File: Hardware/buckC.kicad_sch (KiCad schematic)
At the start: 33 parts, among them Q1 SSM3K15AMFV,L3F, U6 SiC437BED-T1-GE3

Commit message: Maybe chad v3.0 hardware
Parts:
- added C18: TBD, Capacitor_SMD:C_0603_1608Metric, symbol Device:C_Small
- added C19: 47uF, Capacitor_SMD:C_1206_3216Metric, symbol Device:C_Small
- added R42: TBD, Resistor_SMD:R_0603_1608Metric, symbol Device:R_Small
- C31, C34, C36, C40, C41, C42, C43, C44, C47, C49: value DNP -> 47uF; now not fitted
- C46, C48: value DNP -> 47uF; footprint Capacitor_SMD:C_0805_2012Metric -> Capacitor_SMD:C_1206_3216Metric; now not fitted
- L4: MPN (none) -> SPM10065VT-3R3M-D
- U6: value SiC437BED-T1-GE3 -> SiC437AED-T1
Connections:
- net +6V: now also C19.2
- net GND: now also C19.1, R42.2
- net SW: now also C18.1
- net +12V renamed +16.8V
- new net: C18.2, R42.1
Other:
- note added: "RC Snubber"
- moved on the sheet: Q1, R38, R39

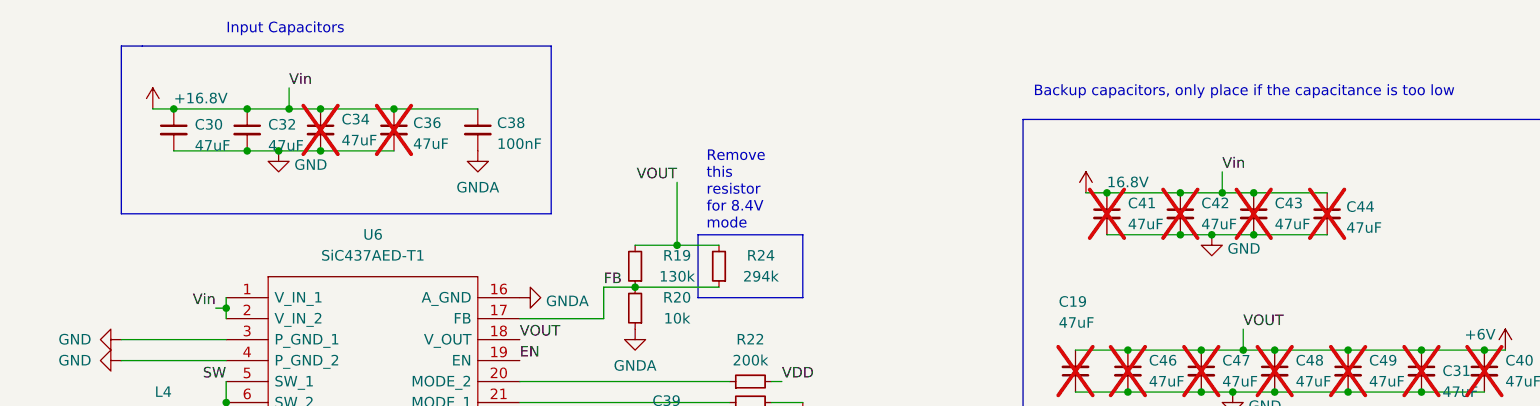
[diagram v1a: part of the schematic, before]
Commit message: 30V compatibility update
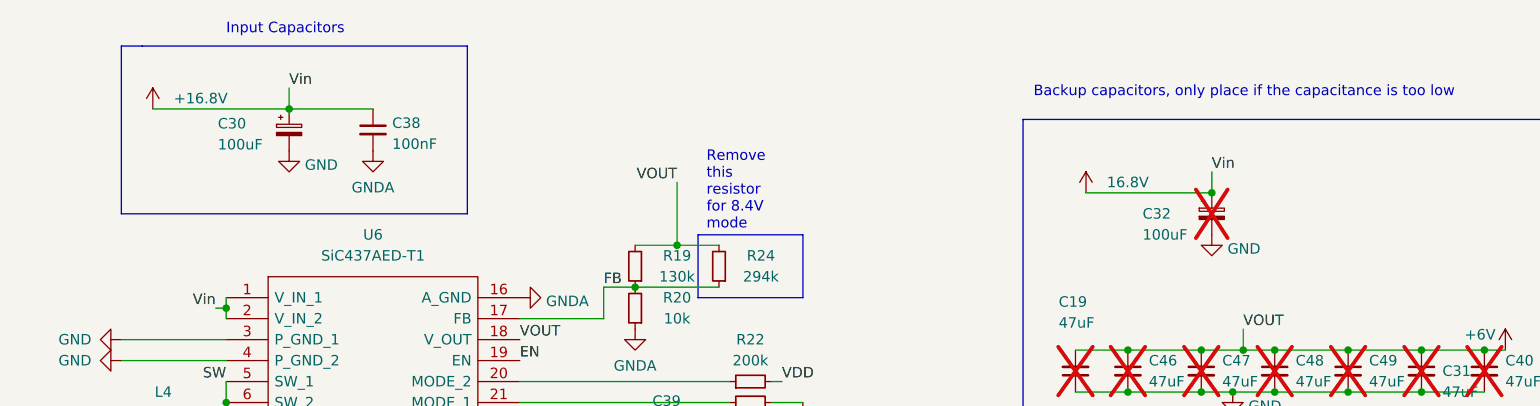
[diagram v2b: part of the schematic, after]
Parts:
- removed C30, C32, C34, C36, C41, C42, C43, C44: 47uF, Capacitor_SMD:C_1206_3216Metric, symbol Device:C_Small
- added C30, C32: 100uF, Capacitor_Tantalum_SMD:CP_EIA-7360-38_Kemet-E, symbol Device:C_Polarized_Small
- Q1: footprint Package_TO_SOT_SMD:SOT-723 -> iclr:SOT-723
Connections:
- net +16.8V: now also C30.1, C32.1
- net GND: now also C30.2, C32.2
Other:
- moved on the sheet: C38

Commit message: Resistor values
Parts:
- R19: value 130k -> 113k; MPN (none) -> ERJ-2RKF1133X
- R24: value 294k -> 442k; MPN (none) -> ERJ-2RKF4423X
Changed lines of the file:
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@@
 			)
 		)
-		(property "Value" "130k"
+		(property "Value" "113k"
 			(at 129.54 48.2569 0)
 			(effects
@@
 		)
 		(property "Description" ""
+			(at 124.46 46.99 0)
+			(effects
+				(font
+					(size 1.27 1.27)
+				)
+				(hide yes)
+			)
+		)
+		(property "MPN" "ERJ-2RKF1133X"
 			(at 124.46 46.99 0)
 			(effects
@@
 			)
 		)
-		(property "Value" "294k"
+		(property "Value" "442k"
 			(at 139.7 48.2569 0)
 			(effects
@@
 			(at 134.62 46.99 0)
 			(effects
+				(font
+					(size 1.27 1.27)
+				)
+				(hide yes)
+			)
+		)
+		(property "MPN" " ERJ-2RKF4423X "
+			(at 134.62 46.99 0)
+			(effects

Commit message: Added GPIO TVS protection
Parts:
- C18: value TBD -> 160pF
- R42: value TBD -> 5.4R
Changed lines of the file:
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@@
 			)
 		)
-		(property "Value" "TBD"
+		(property "Value" "160pF"
 			(at 179.07 86.3662 0)
 			(effects
@@
 			)
 		)
-		(property "Value" "TBD"
+		(property "Value" "5.4R"
 			(at 179.07 91.4399 0)
 			(effects

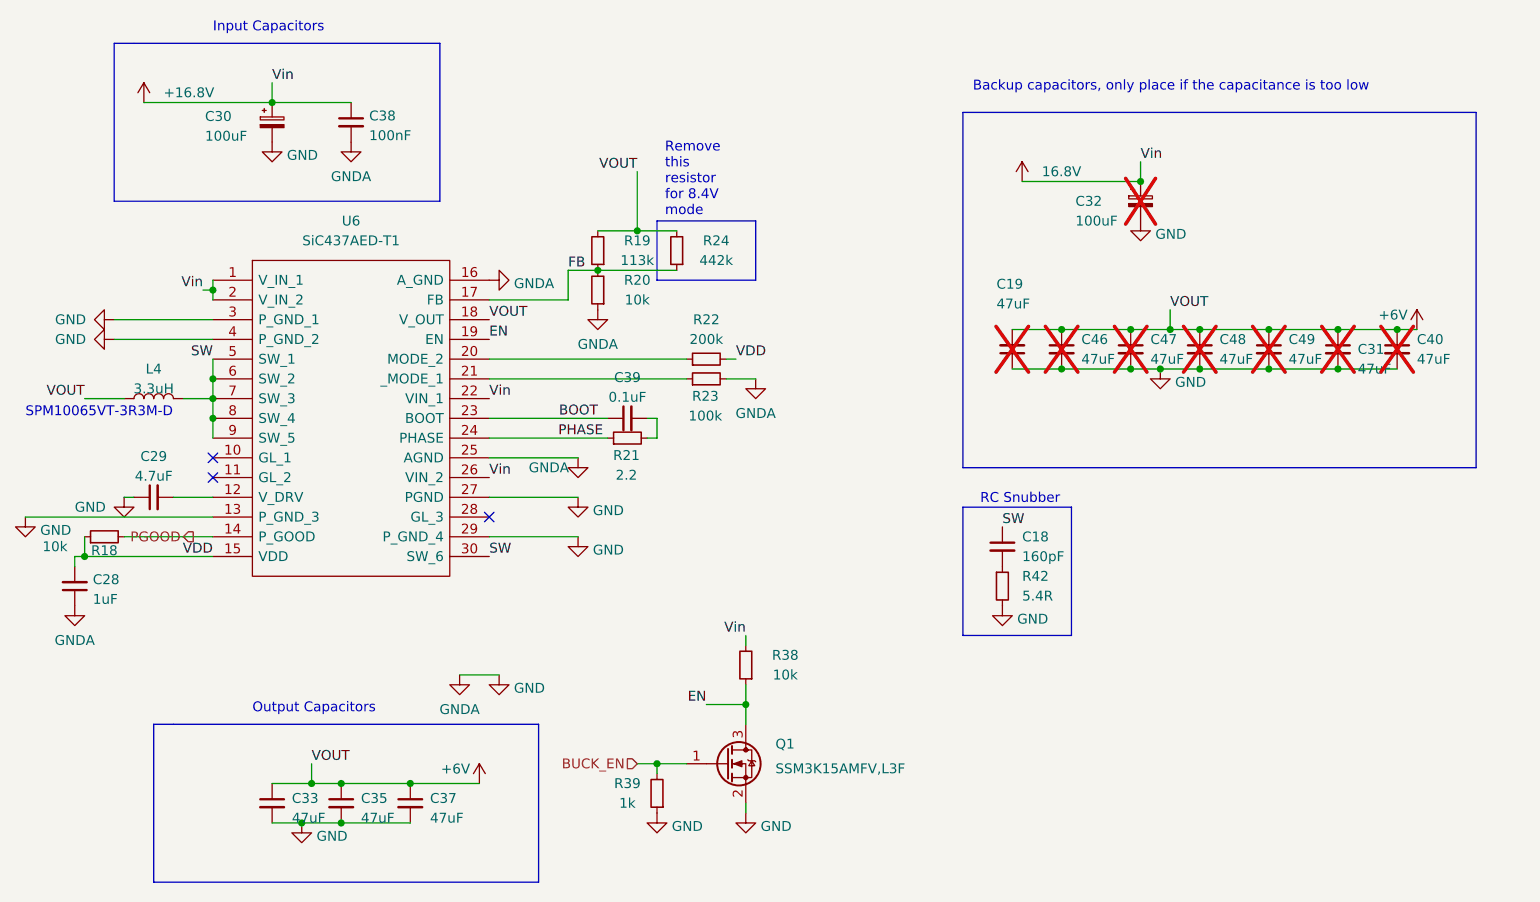
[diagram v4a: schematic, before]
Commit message: fixed pgood hardware issue
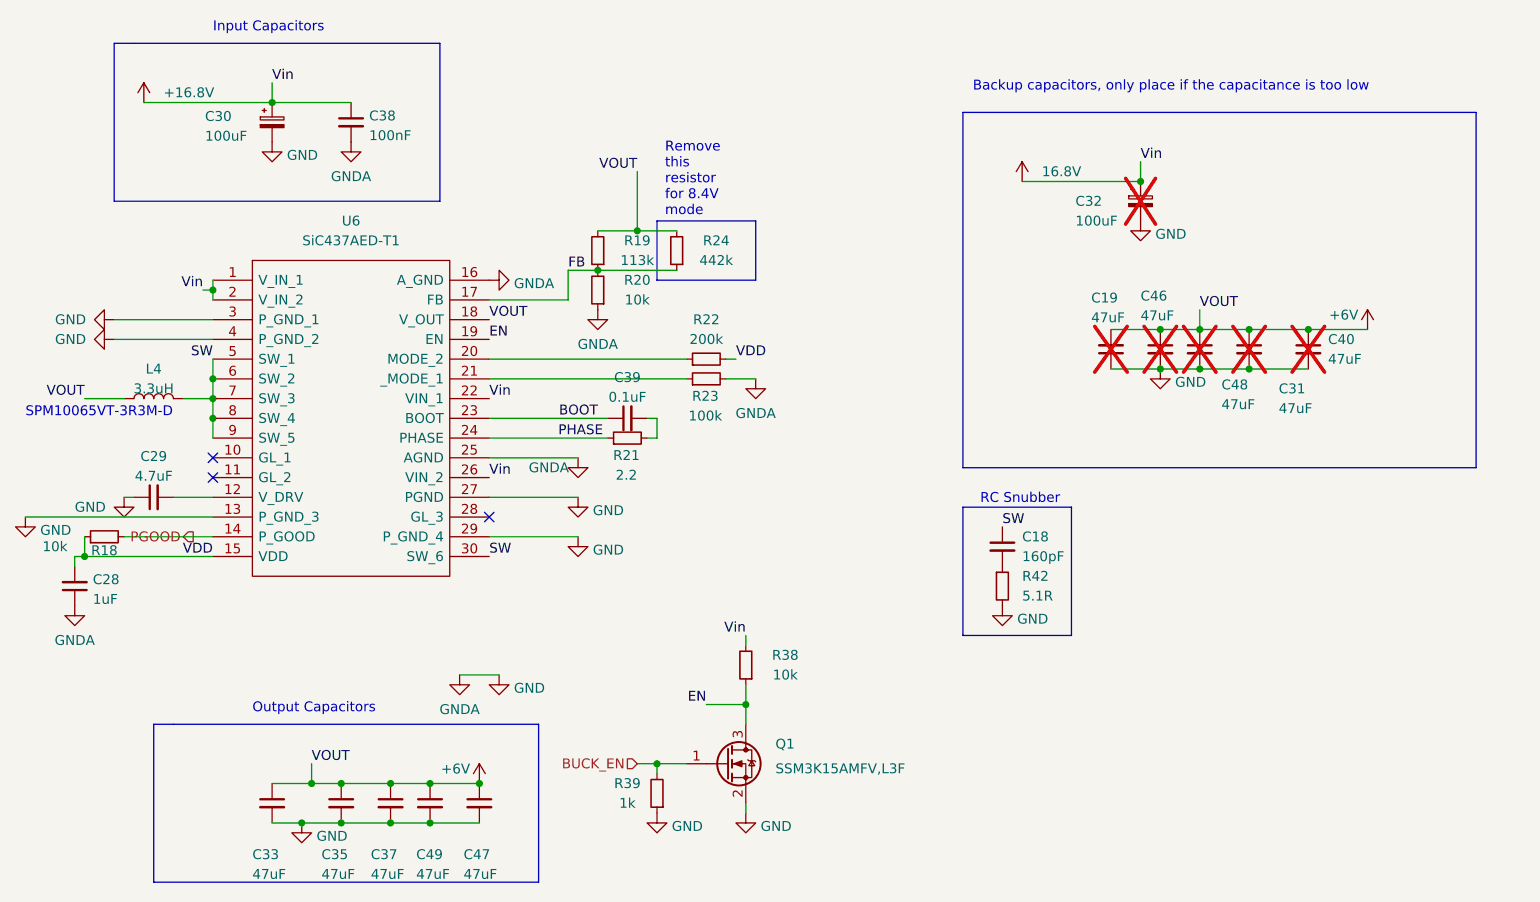
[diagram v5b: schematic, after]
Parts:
- C47, C49: now fitted
- R42: value 5.4R -> 5.1R
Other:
- moved on the sheet: C19, C31, C37, C40, C46

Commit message: cleaned up schematic and bom
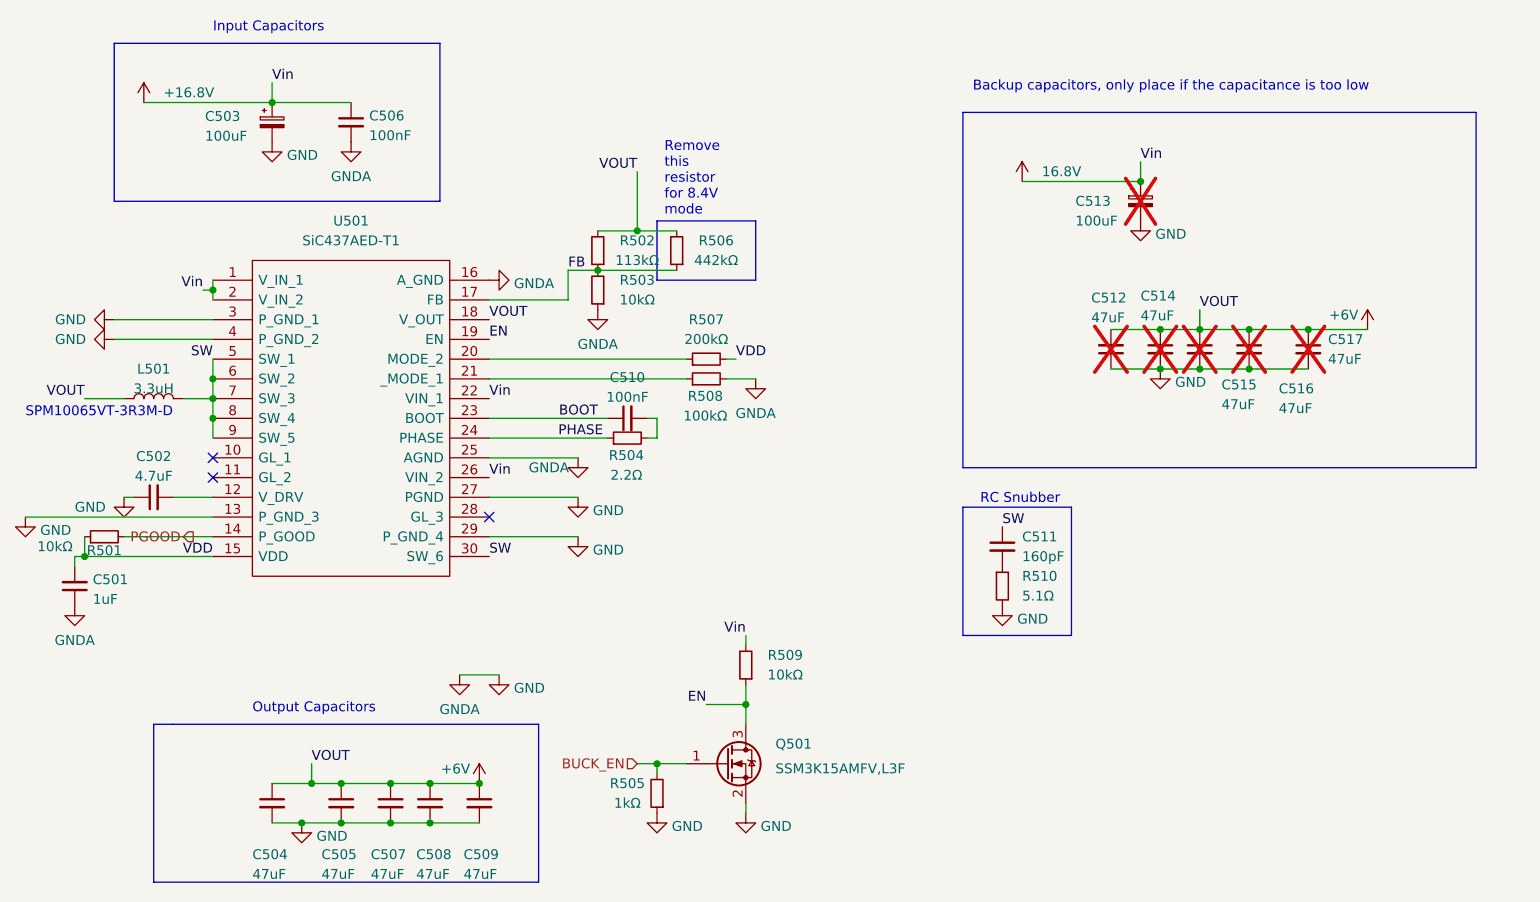
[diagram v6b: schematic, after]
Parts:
- C510: renamed from C39; value 0.1uF -> 100nF
- R501: renamed from R18; value 10k -> 10kΩ
- R502: renamed from R19; value 113k -> 113kΩ
- R503: renamed from R20; value 10k -> 10kΩ
- R504: renamed from R21; value 2.2 -> 2.2Ω
- R505: renamed from R39; value 1k -> 1kΩ
- R506: renamed from R24; value 442k -> 442kΩ
- R507: renamed from R22; value 200k -> 200kΩ
- R508: renamed from R23; value 100k -> 100kΩ
- R509: renamed from R38; value 10k -> 10kΩ
- R510: renamed from R42; value 5.1R -> 5.1Ω
- renumbered C28 to C501, C29 to C502, C30 to C503, C33 to C504, C35 to C505, C38 to C506, C37 to C507, C49 to C508, C47 to C509, C18 to C511, C19 to C512, C32 to C513, C46 to C514, C48 to C515, C31 to C516, C40 to C517, L4 to L501, Q1 to Q501, U6 to U501

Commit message: continued
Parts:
- Q501: footprint iclr:SOT-723 -> Package_TO_SOT_SMD:SOT-723
- U501: value SiC437AED-T1 -> SIC437AED-T1-GE3
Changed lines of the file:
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@@
 			)
 		)
-		(property "Value" "SiC437AED-T1"
+		(property "Value" "SIC437AED-T1-GE3"
 			(at 92.71 45.72 0)
 			(effects
@@
 			)
 		)
-		(property "Footprint" "iclr:SOT-723"
+		(property "Footprint" "Package_TO_SOT_SMD:SOT-723"
 			(at 146.05 110.49 0)
 			(effects
